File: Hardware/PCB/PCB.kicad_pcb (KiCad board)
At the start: 2 copper layers, 2 parts, among them P1 USB_C_Plug_USB2.0, U1 ESP32-H2-MINI-1

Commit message: Playing with LDOs
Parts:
- added U3: AMS1117-3.3, Package_TO_SOT_SMD:SOT-223-3_TabPin2, F.Cu at (119.0, 64.4)
- moved U1 10.4 mm to (150.8, 65.0), turned to -90 degrees
- moved P1 9.94 mm to (107.1, 64.7), turned to -90 degrees
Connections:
- P1 pad A12: Net-(P1-GND-PadA1) -> GND
- P1 pad B12: Net-(P1-GND-PadA1) -> GND
- U1 pad 1: Net-(U1-GND-Pad1) -> GND
- U1 pad 11: Net-(U1-GND-Pad1) -> GND
- U1 pad 14: Net-(U1-GND-Pad1) -> GND
- U1 pad 2: Net-(U1-GND-Pad1) -> GND
- U1 pad 26: unconnected-(U1-GPIO26/FSPICS4/USB_D--Pad26) -> /USB_D-
- U1 pad 27: unconnected-(U1-GPIO27/FSPICS5/USB_D+-Pad27) -> /USB_D+
- U1 pad 3: unconnected-(U1-3V3-Pad3) -> Net-(U1-3V3)
- U1 pad 36: Net-(U1-GND-Pad1) -> GND
- U1 pad 37: Net-(U1-GND-Pad1) -> GND
- U1 pad 38: Net-(U1-GND-Pad1) -> GND
- U1 pad 39: Net-(U1-GND-Pad1) -> GND
- U1 pad 40: Net-(U1-GND-Pad1) -> GND
- U1 pad 41: Net-(U1-GND-Pad1) -> GND
- U1 pad 42: Net-(U1-GND-Pad1) -> GND
- U1 pad 43: Net-(U1-GND-Pad1) -> GND
- U1 pad 44: Net-(U1-GND-Pad1) -> GND
- U1 pad 45: Net-(U1-GND-Pad1) -> GND
- U1 pad 46: Net-(U1-GND-Pad1) -> GND
- U1 pad 47: Net-(U1-GND-Pad1) -> GND
- U1 pad 48: Net-(U1-GND-Pad1) -> GND
- U1 pad 49: Net-(U1-GND-Pad1) -> GND
- U1 pad 50: Net-(U1-GND-Pad1) -> GND
- U1 pad 51: Net-(U1-GND-Pad1) -> GND
- U1 pad 52: Net-(U1-GND-Pad1) -> GND
- U1 pad 53: Net-(U1-GND-Pad1) -> GND
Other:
- board outline added: 50.2 x 30.8 mm

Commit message: First pass at full layout
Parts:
- removed P1: USB_C_Plug_USB2.0, Connector_USB:USB_C_Receptacle_GCT_USB4135-GF-A_6P_TopMnt_Horizontal
- added C1: 10µ, Capacitor_SMD:C_0805_2012Metric, F.Cu at (97.3, 54.6)
- added C2: 1µF, Capacitor_SMD:C_0805_2012Metric, F.Cu at (99.6, 54.6)
- added C3: 0.1µ, Capacitor_SMD:C_0805_2012Metric, F.Cu at (101.9, 54.6)
- added C5: 1µ, Capacitor_SMD:C_0805_2012Metric, F.Cu at (96.0, 65.0)
- added C7: 1µF, Capacitor_SMD:C_0805_2012Metric, F.Cu at (107.3, 63.7)
- added D1: LED, LED_SMD:LED_0805_2012Metric, F.Cu at (114.5, 60.6)
- added D2: LED, LED_SMD:LED_0805_2012Metric, F.Cu at (114.6, 58.2)
- added D3: LED, LED_SMD:LED_0805_2012Metric, F.Cu at (114.6, 55.9)
- added J1: USB_C_Receptacle_USB2.0_14P, Connector_USB:USB_C_Receptacle_GCT_USB4110, F.Cu at (106.3, 71.2)
- added J2: Conn_01x08_Pin, Connector_PinHeader_2.54mm:PinHeader_1x08_P2.54mm_Vertical, F.Cu at (92.0, 41.5)
- added J3: Conn_01x8_Pin, Connector_PinHeader_2.54mm:PinHeader_1x08_P2.54mm_Vertical, F.Cu at (120.3, 41.9)
- added R1: 5.1K, Resistor_SMD:R_0805_2012Metric, F.Cu at (113.8, 64.3)
- added R2: 5.1K, Resistor_SMD:R_0805_2012Metric, F.Cu at (101.1, 64.1)
- added R3: 10K, Resistor_SMD:R_0805_2012Metric, F.Cu at (95.9, 61.5)
- added R4: 5.1K, Resistor_SMD:R_0805_2012Metric, F.Cu at (110.6, 60.5)
- added R5: 5.1K, Resistor_SMD:R_0805_2012Metric, F.Cu at (110.6, 58.2)
- added R6: 5.1K, Resistor_SMD:R_0805_2012Metric, F.Cu at (110.6, 55.9)
- added SW1: SW_Push, Button_Switch_SMD:SW_SPST_TS-1088-xR025, F.Cu at (96.9, 70.2)
- added SW2: SW_Push, Button_Switch_SMD:SW_SPST_TS-1088-xR025, F.Cu at (115.8, 70.2)
- U3: value AMS1117-3.3 -> MCP1700x-330xxTT; footprint Package_TO_SOT_SMD:SOT-223-3_TabPin2 -> Package_TO_SOT_SMD:SOT-23
- moved U1 50.5 mm to (105.6, 42.4), turned to 0 degrees
- moved U3 15.1 mm to (104.4, 60.6), turned to -90 degrees
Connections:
- net Net-(U1-3V3) renamed +3.3V
- U1 pad 10: unconnected-(U1-GPIO1/FSPICS0/ADC1_CH0-Pad10) -> GPIO1
- U1 pad 12: unconnected-(U1-GPIO13/XTAL_32K_P-Pad12) -> GPIO13
- U1 pad 13: unconnected-(U1-GPIO14/XTAL_32K_N-Pad13) -> GPIO14
- U1 pad 16: unconnected-(U1-GPIO12-Pad16) -> GPIO12
- U1 pad 18: unconnected-(U1-GPIO4/FSPICLK/ADC1_CH3/MTCK-Pad18) -> GPIO4
- U1 pad 19: unconnected-(U1-GPIO5/FSPID/ADC1_CH4/MTDI-Pad19) -> GPIO5
- U1 pad 20: unconnected-(U1-GPIO10/ZCD0-Pad20) -> GPIO10
- U1 pad 21: unconnected-(U1-GPIO11/ZCD1-Pad21) -> GPIO11
- U1 pad 22: unconnected-(U1-GPIO8-Pad22) -> GPIO8
- U1 pad 23: unconnected-(U1-GPIO9-Pad23) -> GPIO9
- U1 pad 24: unconnected-(U1-GPIO22-Pad24) -> GPIO22
- U1 pad 25: unconnected-(U1-GPIO25/FSPICS3-Pad25) -> GPIO25
- U1 pad 26: /USB_D- -> USB_D-
- U1 pad 27: /USB_D+ -> USB_D+
- U1 pad 30: unconnected-(U1-GPIO23/FSPICS1/U0RXD-Pad30) -> GPIO23
- U1 pad 31: unconnected-(U1-GPIO24/FSPICS2/U0TXD-Pad31) -> GPIO24
- U1 pad 5: unconnected-(U1-GPIO2/FSPIWP/ADC1_CH1/MTMS-Pad5) -> GPIO2
- U1 pad 6: unconnected-(U1-GPIO3/FSPIHD/ADC1_CH2/MTDO-Pad6) -> GPIO3
- U1 pad 8: unconnected-(U1-EN-Pad8) -> EN
- U1 pad 9: unconnected-(U1-GPIO0/FSPIQ-Pad9) -> BOOT
- U3 pad 3: Net-(U3-VI) -> +5V
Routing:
- net GND: track 0.00 -> 114.8 mm, vias 0 -> 5
- net +5V: track 0.00 -> 61.2 mm, vias 0 -> 3
- net +3.3V: track 0.00 -> 49.5 mm, vias 0 -> 2
- net BOOT: track 0.00 -> 33.8 mm, vias 0 -> 2
- net USB_D+: track 0.00 -> 26.3 mm, vias 0 -> 2
- net USB_D-: track 0.00 -> 25.2 mm, vias 0 -> 2
- net EN: track 0.00 -> 24.8 mm, vias 0 -> 2
- net GPIO5: track 0.00 -> 18.8 mm
- net GPIO12: track 0.00 -> 17.1 mm
- net GPIO10: track 0.00 -> 16.3 mm
- net GPIO11: track 0.00 -> 14.6 mm
- net GPIO8: track 0.00 -> 13.5 mm
- net GPIO22: track 0.00 -> 13.4 mm
- net GPIO9: track 0.00 -> 13.4 mm
- net GPIO14: track 0.00 -> 12.7 mm
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- added copper zone on B.Cu, net GND
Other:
- board size 50.2 x 30.8 mm -> 32.7 x 35.8 mm

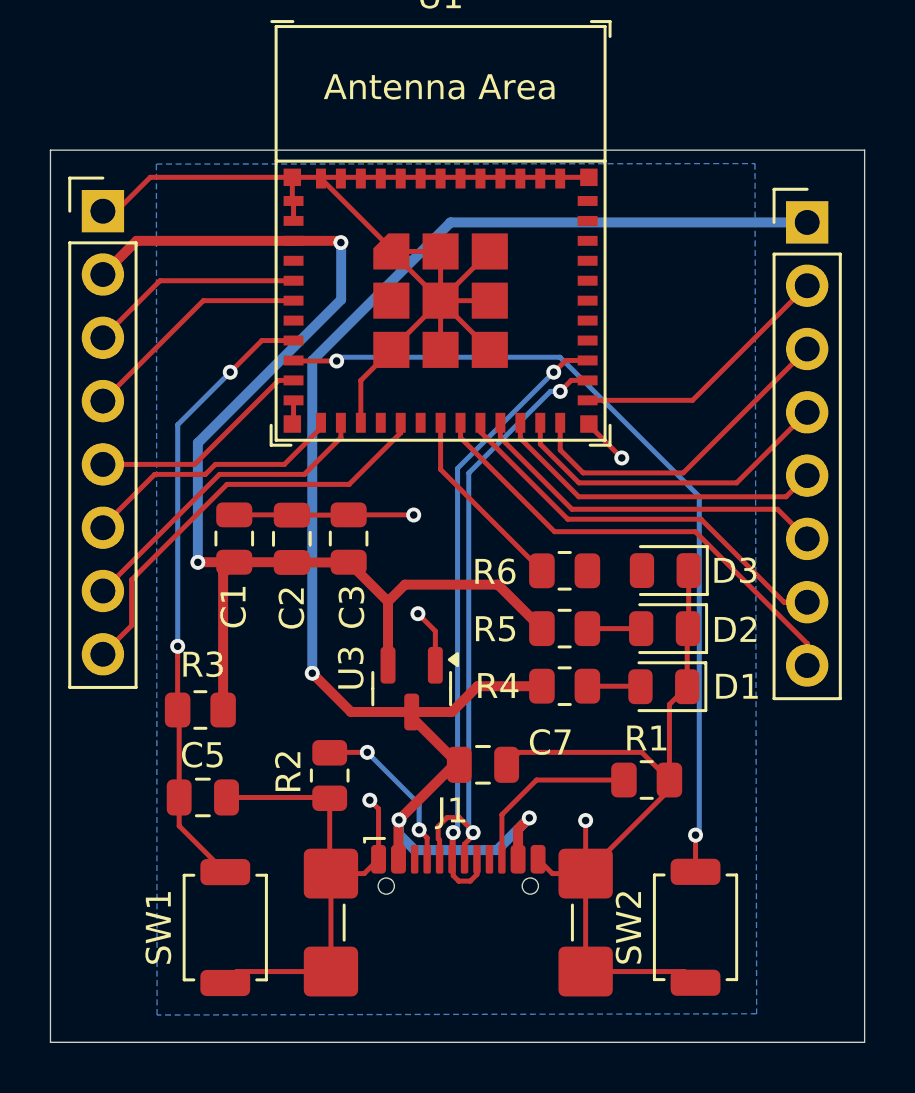
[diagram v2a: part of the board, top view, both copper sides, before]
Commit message: Finished PCB layout
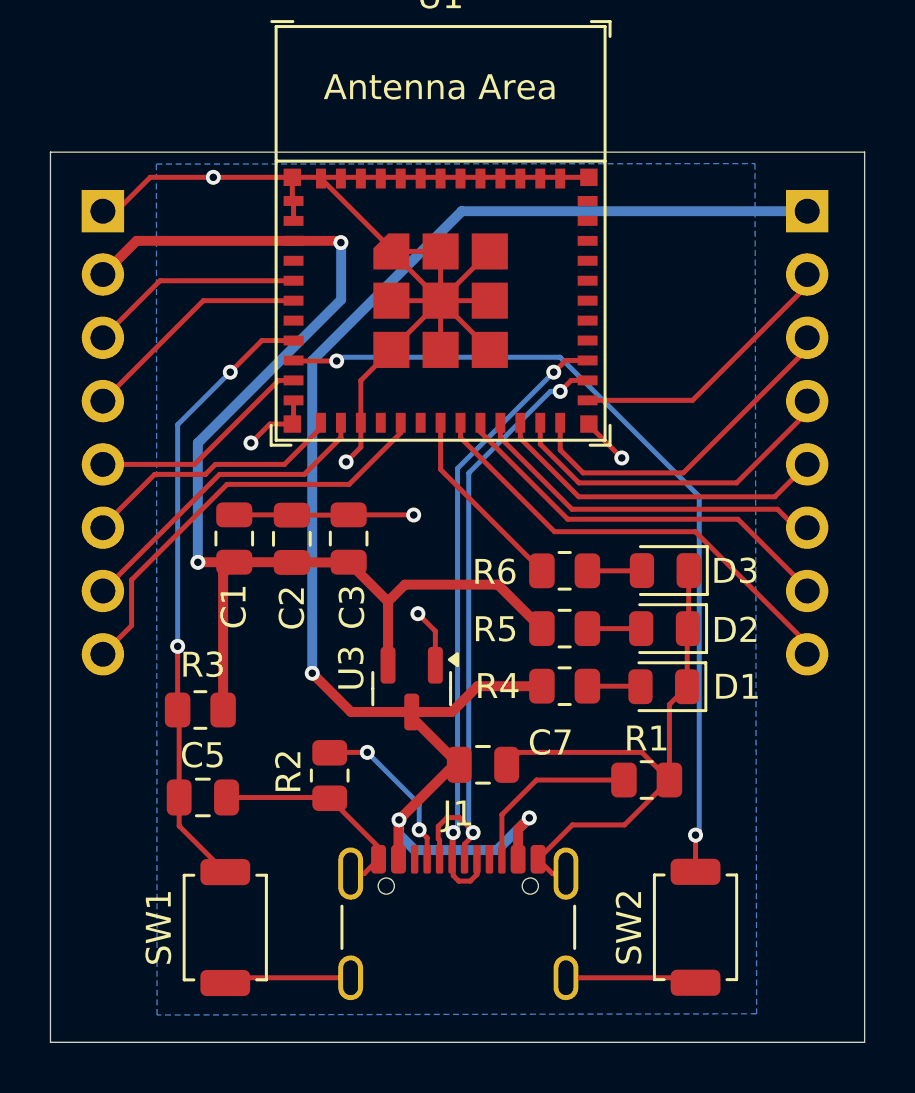
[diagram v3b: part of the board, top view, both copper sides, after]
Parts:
- J1: footprint Connector_USB:USB_C_Receptacle_GCT_USB4110 -> Connector_USB:USB_C_Receptacle_GCT_USB4105-xx-A_16P_TopMnt_Horizontal
- J2, J3: moved to B.Cu
- moved J3 0.45 mm to (120.3, 41.5), turned to 180 degrees
- turned J2 to 180 degrees
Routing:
- net GND: track 114.8 -> 110.0 mm, vias 5 -> 6
- net Net-(D3-A): track 0.00 -> 2.19 mm
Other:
- board size 32.7 x 35.8 mm -> 32.7 x 35.7 mm

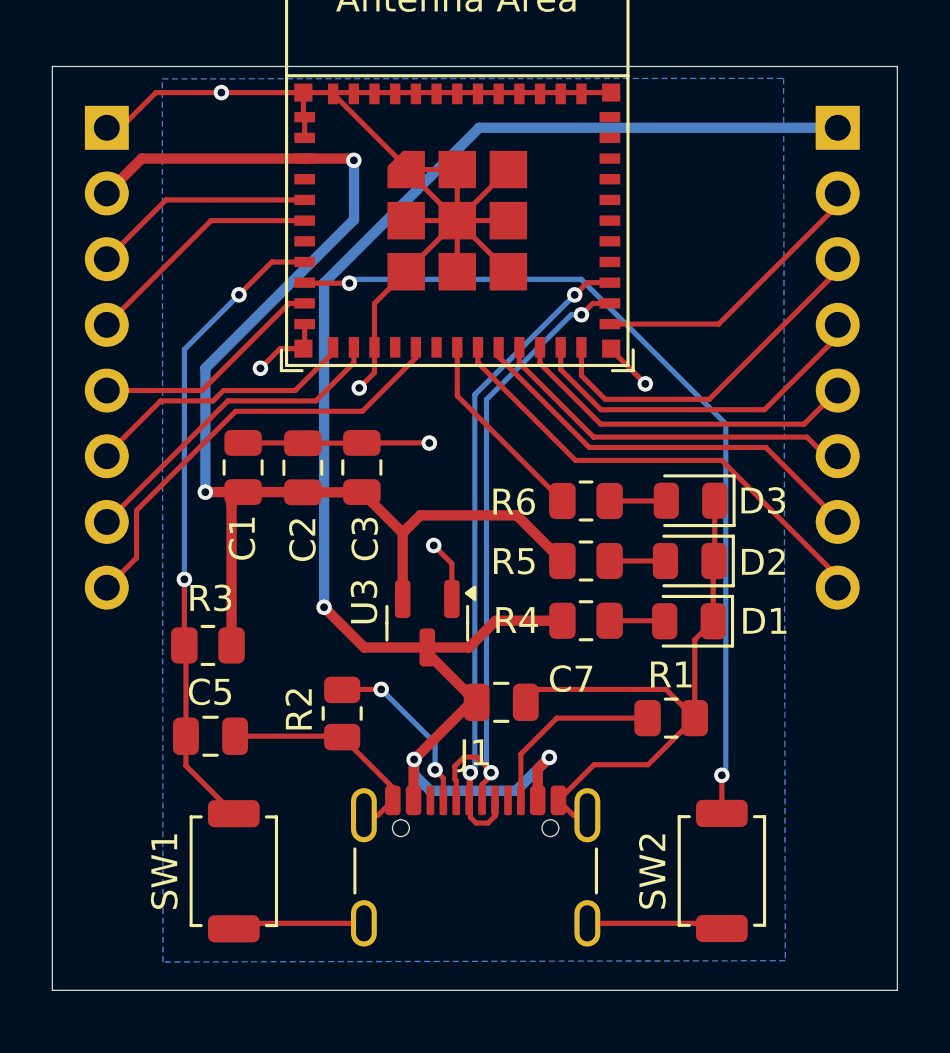
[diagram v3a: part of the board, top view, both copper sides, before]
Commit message: Fixed up RC capacitor order
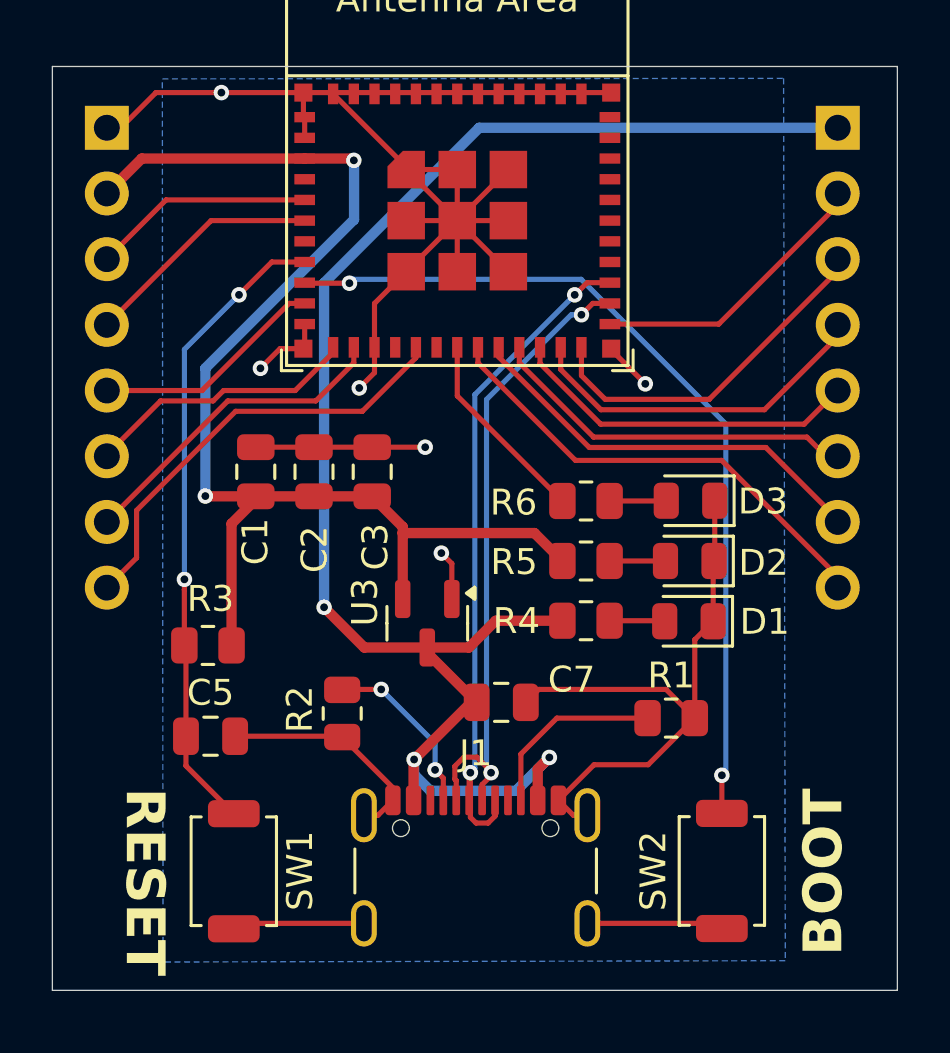
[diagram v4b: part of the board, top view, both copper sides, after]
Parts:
- C1: value 10µ -> 0.1µ
- C2: value 1µF -> 10µ
- C3: value 0.1µ -> 1µF
- moved C1 0.52 mm to (97.8, 54.8)
- moved C2 0.46 mm to (100.0, 54.8)
- moved C3 0.43 mm to (102.3, 54.8)
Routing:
- net GND: track 110.0 -> 108.5 mm
- net GPIO5: track 18.8 -> 17.9 mm
- net GPIO10: track 16.7 -> 16.1 mm
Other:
- board text added: "@tomasmcguinness"
- board text added: "BOOT"
- board text added: "ESP32-H2 DevKit"
- board text added: "RESET"
- board text added: "v${REVISION}"
